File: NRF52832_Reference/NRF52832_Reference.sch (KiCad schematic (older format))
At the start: 22 parts

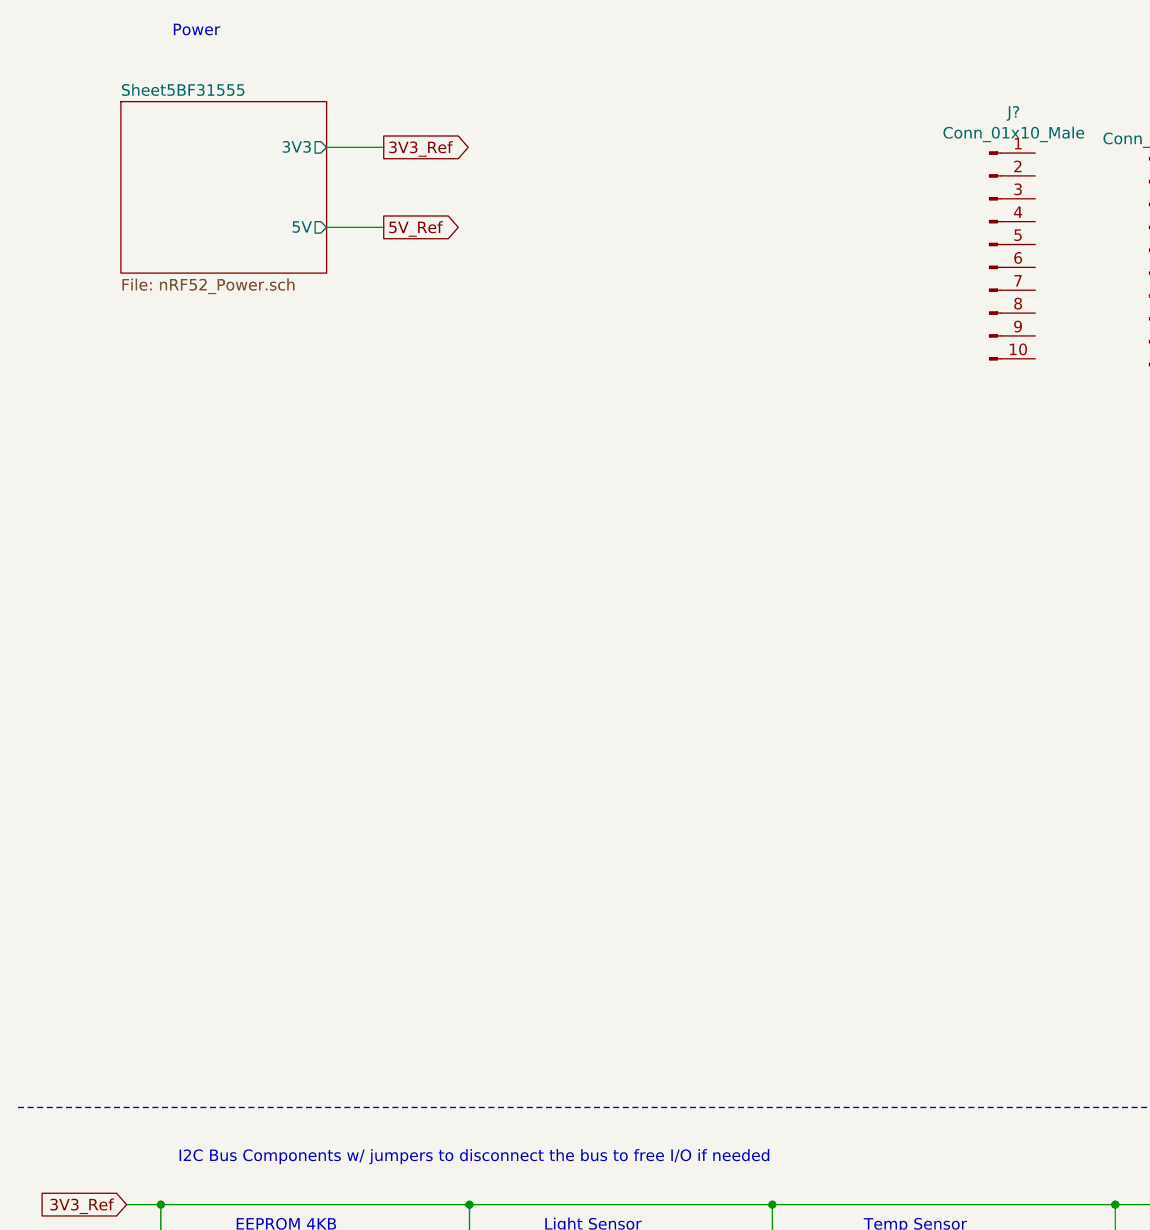
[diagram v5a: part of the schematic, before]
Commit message: Added LCD with SPI interface to schematic.
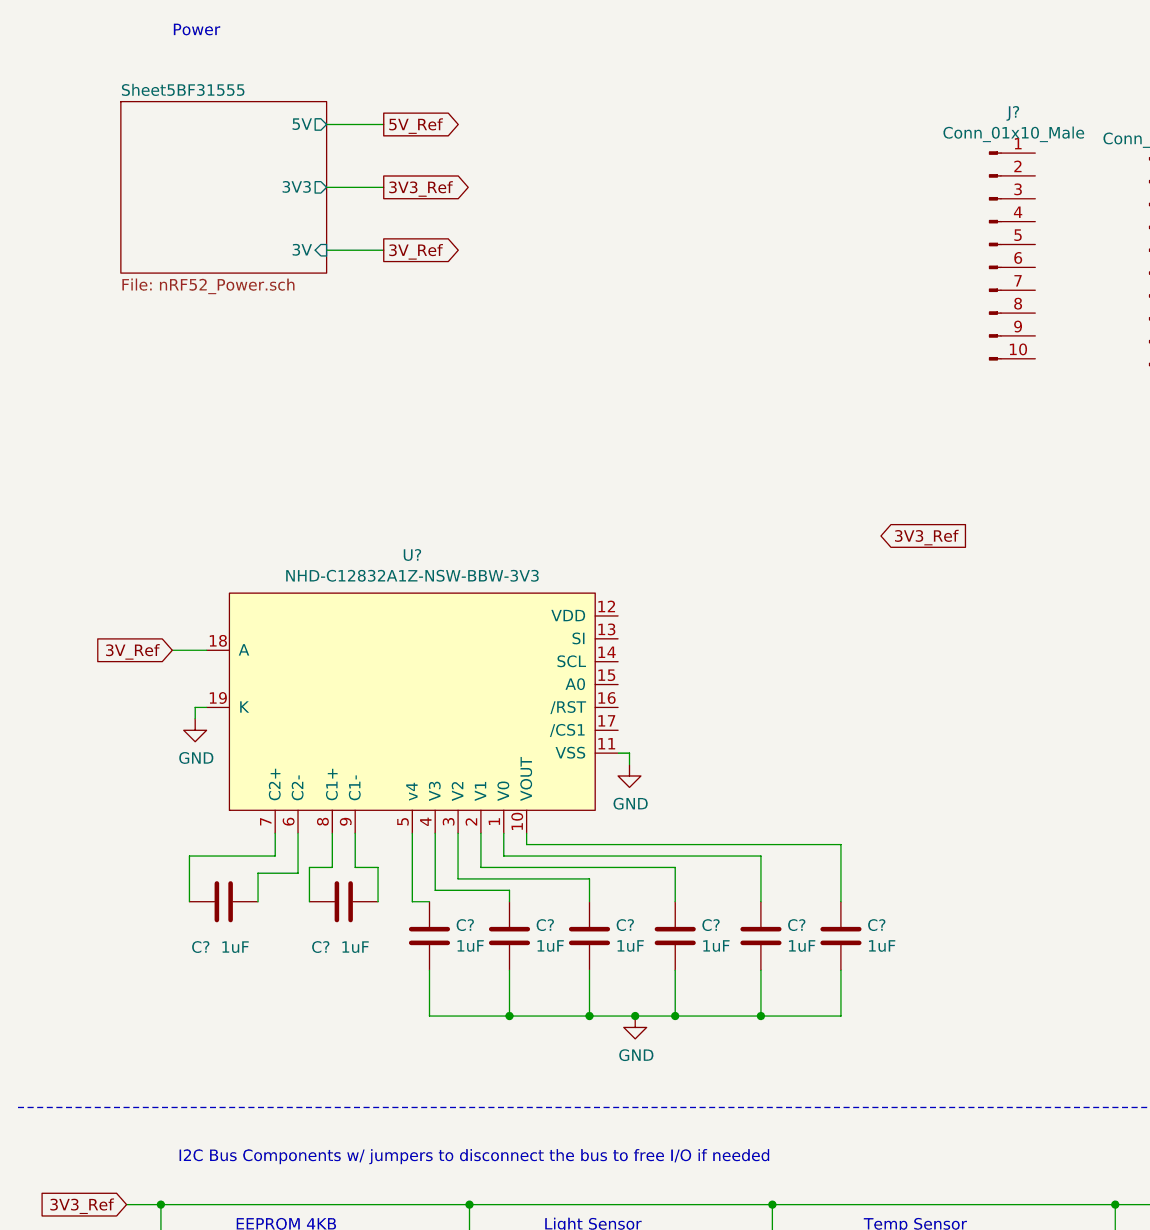
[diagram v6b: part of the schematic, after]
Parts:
- added C? (x8): 1uF, symbol Device:C
- added U?: NHD-C12832A1Z-NSW-BBW-3V3, symbol Project_Libary:NHD-C12832A1Z-NSW-BBW-3V3
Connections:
- net GND: now also C?.2, C?.2, C?.2, C?.2, C?.2, C?.2, U?.11 (VSS), U?.19 (K)
- new net: C?.1, U?.1 (V0)
- new net: C?.1, U?.10 (VOUT)
- new net: C?.1, U?.2 (V1)
- new net: C?.1, U?.3 (V2)
- new net: C?.1, U?.4 (V3)
- new net: C?.1, U?.5 (v4)
- new net: C?.1, U?.6 (C2-)
- new net: C?.2, U?.7 (C2+)
- new net: C?.2, U?.8 (C1+)
- new net: C?.1, U?.9 (C1-)
- new net 3V_Ref: U?.18 (A)

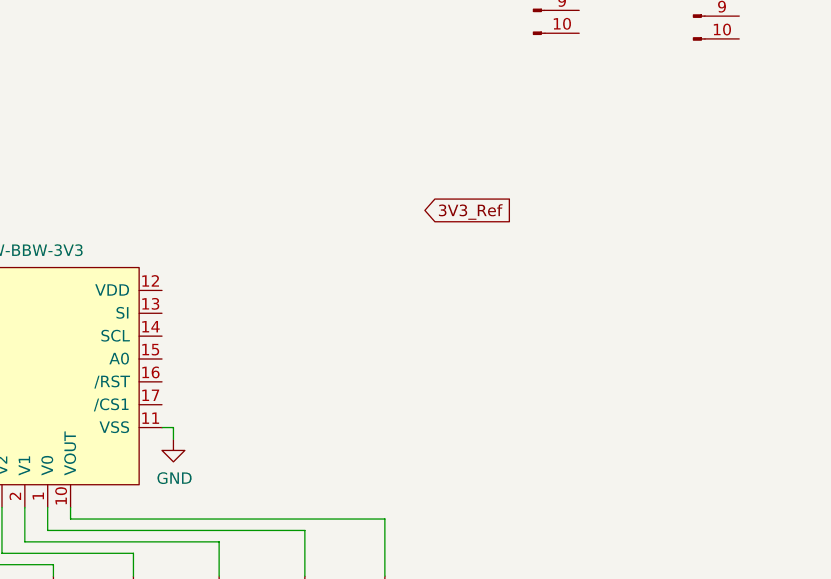
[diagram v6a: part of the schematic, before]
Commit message: Updated LCD circuit schematic.
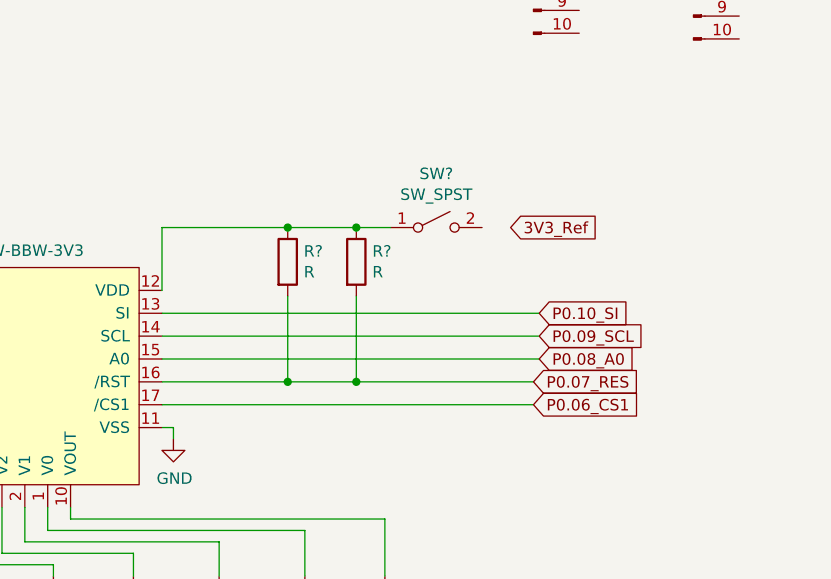
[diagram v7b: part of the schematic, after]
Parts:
- added R? (x2): R, symbol Device:R
- added SW?: SW_SPST, symbol Switch:SW_SPST
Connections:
- net at U?.12 (VDD): now also R?.1, R?.1, SW?.1 (A)
- net P0.10_SI: now reaches U?.13 (SI)
- net P0.09_SCL: now reaches U?.14 (SCL)
- net P0.08_A0: now reaches U?.15 (A0)
- net P0.07_RES: now reaches U?.16 (/RST)
- net P0.07_RES: now also R?.2, R?.2
- net P0.06_CS1: now reaches U?.17 (/CS1)
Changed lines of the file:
@@
 Wire Wire Line
 	1250 3675 1250 3725
-Text GLabel 4250 2925 2    50   Input ~ 0
+Text GLabel 4625 3000 2    50   Input ~ 0
 3V3_Ref
+$Comp
+L Device:R R?
+U 1 1 5C0CAB0C
+P 3650 3150
+F 0 "R?" H 3720 3196 50  0000 L CNN
+F 1 "R" H 3720 3105 50  0000 L CNN
+F 2 "" V 3580 3150 50  0001 C CNN
+F 3 "~" H 3650 3150 50  0001 C CNN
+	1    3650 3150
+	1    0    0    -1
+$EndComp
+$Comp
+L Device:R R?
+U 1 1 5C0CAB88
+P 3950 3150
+F 0 "R?" H 4020 3196 50  0000 L CNN
+F 1 "R" H 4020 3105 50  0000 L CNN
+F 2 "" V 3880 3150 50  0001 C CNN
+F 3 "~" H 3950 3150 50  0001 C CNN
+	1    3950 3150
+	1    0    0    -1
+$EndComp
+Wire Wire Line
+	3100 3775 4725 3775
+Wire Wire Line
+	3100 3675 3650 3675
+Text GLabel 4725 3775 2    50   Input ~ 0
+P0.06_CS1
+Text GLabel 4725 3675 2    50   Input ~ 0
+P0.07_RES
+Text GLabel 4750 3575 2    50   Input ~ 0
+P0.08_A0
+Text GLabel 4750 3475 2    50   Input ~ 0
+P0.09_SCL
+Text GLabel 4750 3375 2    50   Input ~ 0
+P0.10_SI
+Wire Wire Line
+	3100 3575 4750 3575
+Wire Wire Line
+	4750 3475 3100 3475
+Wire Wire Line
+	3100 3375 4750 3375
+Wire Wire Line
+	3650 3675 3650 3300
+Connection ~ 3650 3675
+Wire Wire Line
+	3650 3675 3950 3675
+Wire Wire Line
+	3950 3675 3950 3300
+Connection ~ 3950 3675
+Wire Wire Line
+	3950 3675 4725 3675
+Wire Wire Line
+	3100 3275 3100 3000
+Wire Wire Line
+	3100 3000 3650 3000
+Connection ~ 3650 3000
+Wire Wire Line
+	3650 3000 3950 3000
+Connection ~ 3950 3000
+Wire Wire Line
+	3950 3000 4100 3000
+$Comp
+L Switch:SW_SPST SW?
+U 1 1 5C0FC1D4
+P 4300 3000
+F 0 "SW?" H 4300 3235 50  0000 C CNN
+F 1 "SW_SPST" H 4300 3144 50  0000 C CNN
+F 2 "" H 4300 3000 50  0001 C CNN
+F 3 "" H 4300 3000 50  0001 C CNN
+	1    4300 3000
+	1    0    0    -1
+$EndComp
 $EndSCHEMATC

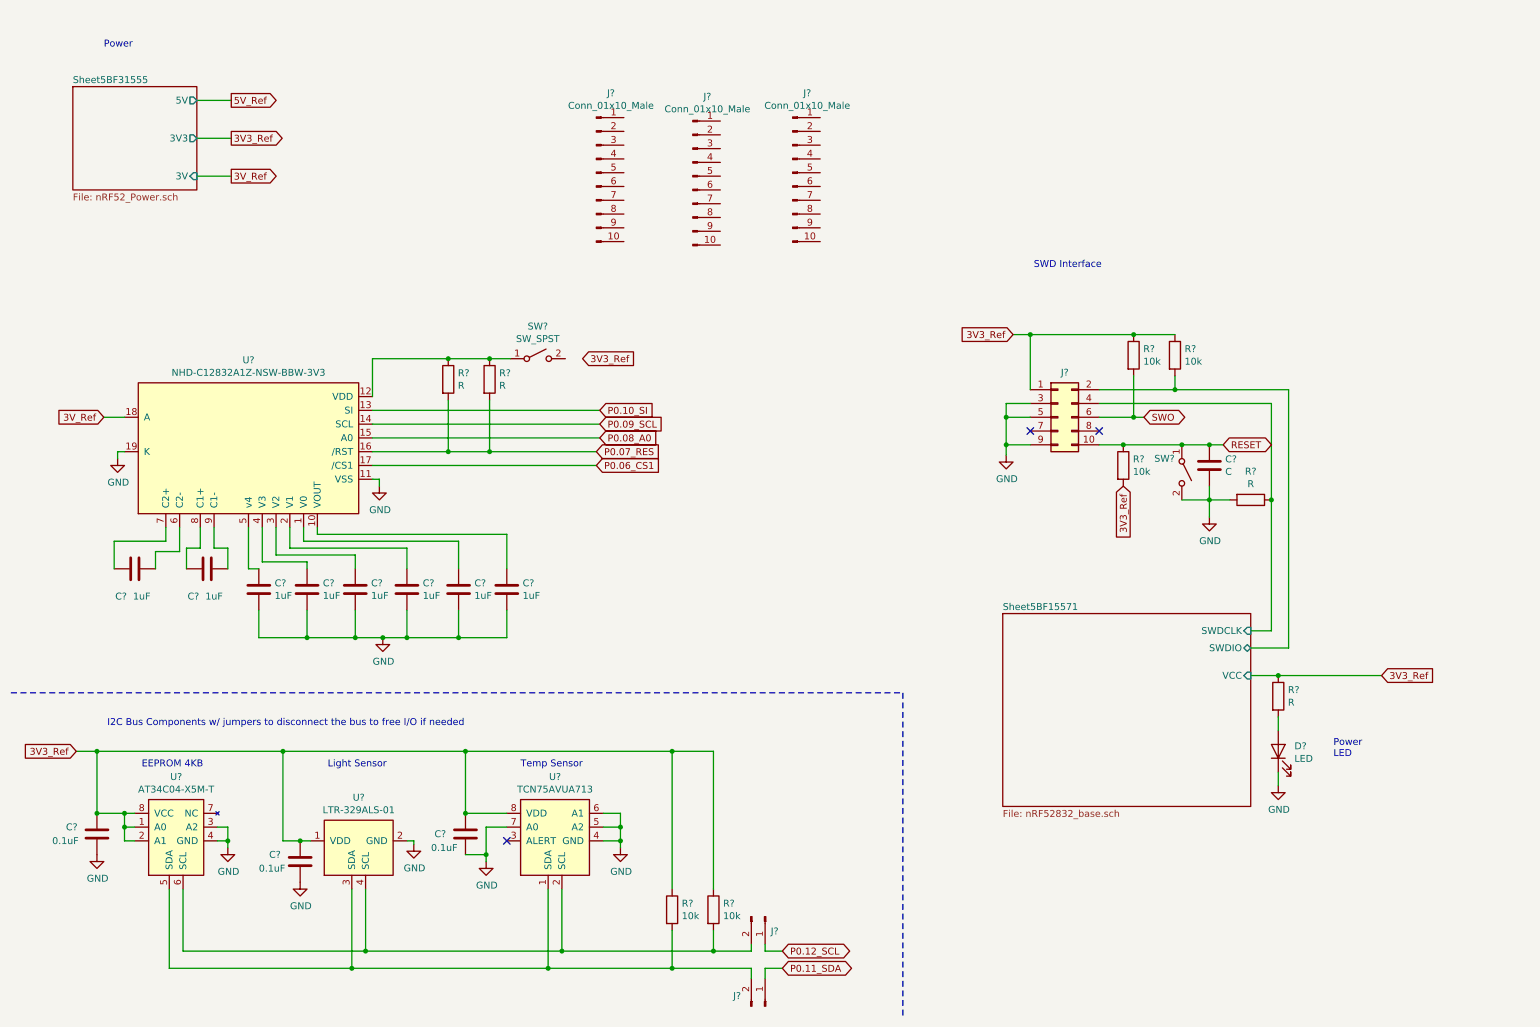
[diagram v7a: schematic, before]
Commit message: Added main power switch and LCD power switch. Added GPIO breakout pins.
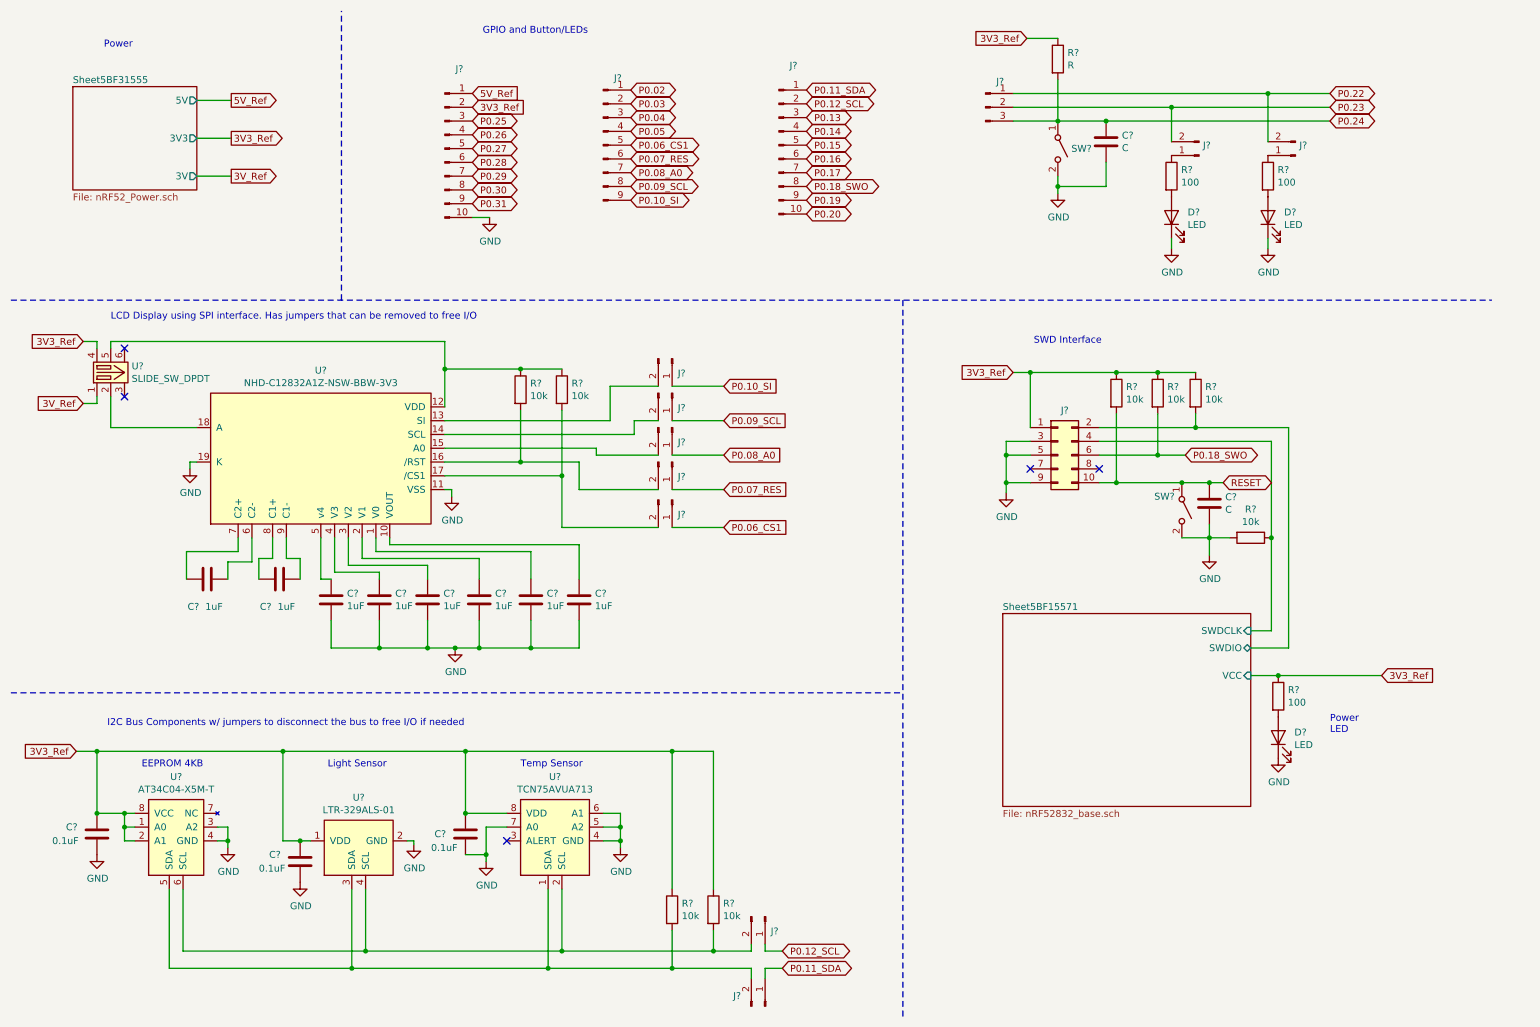
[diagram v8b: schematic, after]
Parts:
- removed J?: Conn_01x10_Male, symbol Connector:Conn_01x10_Male
- removed SW?: SW_SPST, symbol Switch:SW_SPST
- added C?: C, symbol Device:C
- added D? (x2): LED, symbol Device:LED
- added J? (x7): Conn_01x02_Male, symbol Connector:Conn_01x02_Male
- added J?: Conn_01x09_Male, symbol Connector:Conn_01x09_Male
- added J?: Conn_01x03_Male, symbol Connector:Conn_01x03_Male
- added R?: R, symbol Device:R
- added R? (x2): 100, symbol Device:R
- added SW?: SW_SPST, symbol Switch:SW_SPST
- added U?: SLIDE_SW_DPDT, symbol Project_Libary:SLIDE_SW_DPDT
- R?: value R -> 100
- R? (x3): value R -> 10k
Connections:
- net SWO is gone; now on net P0.18_SWO: J?.6 (Pin_6), R?.2
- net 3V3_Ref: now also J?.2 (Pin_2), R?.1, R?.1, U?.4; no longer R?.2
- net 3V_Ref: now also U?.1; no longer U?.18 (A)
- net 5V_Ref: now also J?.1 (Pin_1)
- net GND: now also J?.10 (Pin_10), C?.2, D?.1 (K), D?.1 (K), SW?.2 (B)
- net P0.06_CS1: now also J?.1 (Pin_1), J?.5 (Pin_5); no longer U?.17 (/CS1)
- net P0.07_RES: now also J?.1 (Pin_1), J?.6 (Pin_6); no longer R?.2, R?.2, U?.16 (/RST)
- net P0.08_A0: now also J?.1 (Pin_1), J?.7 (Pin_7); no longer U?.15 (A0)
- net P0.09_SCL: now also J?.1 (Pin_1), J?.8 (Pin_8); no longer U?.14 (SCL)
- net P0.10_SI: now also J?.1 (Pin_1), J?.9 (Pin_9); no longer U?.13 (SI)
- net P0.11_SDA: now also J?.1 (Pin_1)
- net P0.12_SCL: now also J?.2 (Pin_2)
- net RESET: now also R?.2; no longer R?.1
- net P0.25: now reaches J?.3 (Pin_3)
- net P0.26: now reaches J?.4 (Pin_4)
- net P0.27: now reaches J?.5 (Pin_5)
- net P0.28: now reaches J?.6 (Pin_6)
- net P0.29: now reaches J?.7 (Pin_7)
- net P0.30: now reaches J?.8 (Pin_8)
- net P0.31: now reaches J?.9 (Pin_9)
- net P0.20: now reaches J?.10 (Pin_10)
- net P0.13: now reaches J?.3 (Pin_3)
- net P0.14: now reaches J?.4 (Pin_4)
- net P0.15: now reaches J?.5 (Pin_5)
- net P0.16: now reaches J?.6 (Pin_6)
- net P0.17: now reaches J?.7 (Pin_7)
- net P0.18_SWO: now reaches J?.8 (Pin_8)
- net P0.19: now reaches J?.9 (Pin_9)
- net at R?.1, R?.1, U?.12 (VDD): now also U?.5
- new net: J?.2 (Pin_2), U?.13 (SI)
- new net: J?.2 (Pin_2), U?.14 (SCL)
- new net: J?.2 (Pin_2), U?.15 (A0)
- new net: J?.2 (Pin_2), R?.2, U?.16 (/RST)
- new net: J?.2 (Pin_2), R?.2, U?.17 (/CS1)
- new net: U?.18 (A), U?.2
- new net: J?.1 (Pin_1), R?.1 (x2)
- new net: D?.2 (A), R?.2 (x2)
- new net P0.02: J?.1 (Pin_1)
- new net P0.03: J?.2 (Pin_2)
- new net P0.04: J?.3 (Pin_3)
- new net P0.05: J?.4 (Pin_4)
- new net P0.22: J?.1 (Pin_1), J?.2 (Pin_2)
- new net P0.23: J?.2 (Pin_2), J?.2 (Pin_2)
- new net P0.24: C?.1, J?.3 (Pin_3), R?.2, SW?.1 (A)
- no-connect marks 3 -> 5
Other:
- note added: "GPIO and Button/LEDs"
- note added: "LCD Display using SPI interface. Has jumpers that can be removed to free I/O"
- moved on the sheet: C?, D?, J?, R?, SW?, U?
